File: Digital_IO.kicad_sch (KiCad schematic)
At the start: 28 parts, among them J1 MMCX, J10 MMCX, J11 MMCX, J12 MMCX, J13 MMCX, J14 MMCX, J15 MMCX, J16 MMCX, J2 MMCX, J3 MMCX, J4 MMCX, J5 MMCX, J6 MMCX, J7 MMCX, J8 MMCX, J9 MMCX, U44 LP3855EMP-ADJ/NOPB

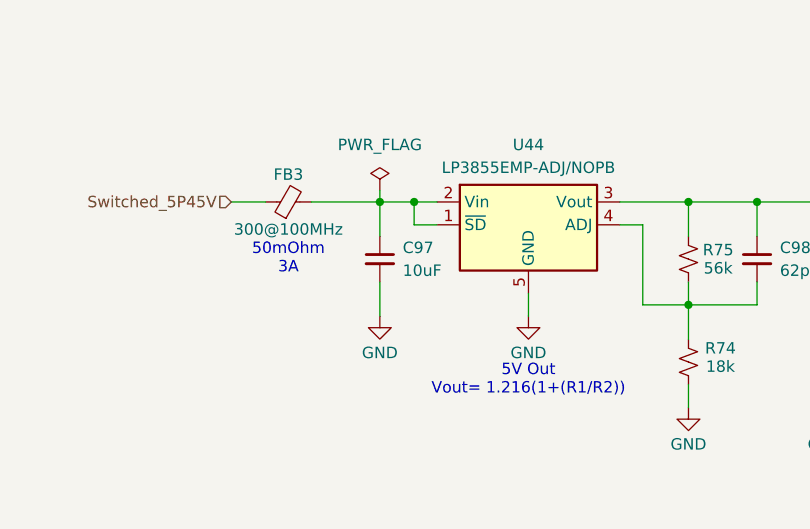
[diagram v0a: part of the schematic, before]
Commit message: Modified Power Filtering
- Removed FB1 & C136
- Added additional 1210 bypassing caps on main power inputs from FMC
- Changed SMPS output caps to the new 1210 22uF part
- Changed Input cap to LD0 U44 to the new 22uF part.
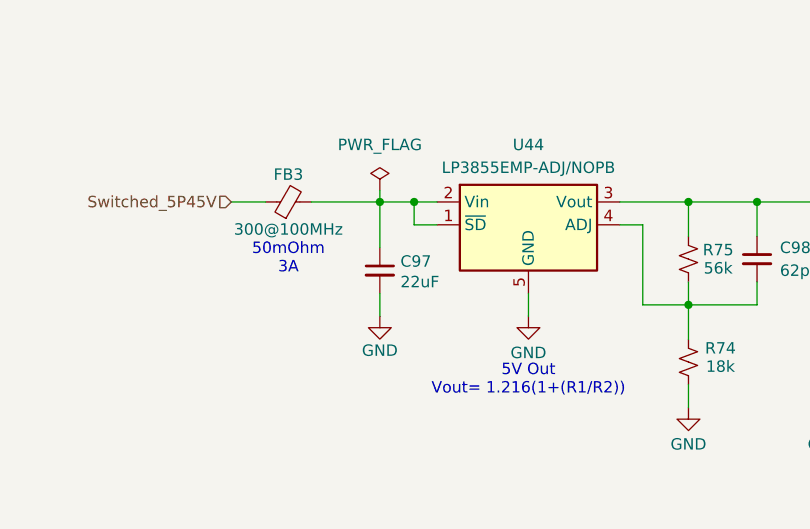
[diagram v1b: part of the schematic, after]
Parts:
- C97: value 10uF -> 22uF; footprint Capacitor_SMD:C_0805_2012Metric -> Capacitor_SMD:C_1210_3225Metric; MPN GRM21BR61E106KA73L -> CL32A226KAJNNWE; Manufacturer Murata -> Samsung Electro-Mechanics
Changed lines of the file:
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@@
 	(wire
 		(pts
+			(xy 54.61 137.16) (xy 54.61 139.7)
+		)
+		(stroke
+			(width 0)
+			(type default)
+		)
+	)
+	(wire
+		(pts
 			(xy 243.84 92.71) (xy 237.49 92.71)
 		)
@@
 	(wire
 		(pts
-			(xy 54.61 135.89) (xy 54.61 139.7)
-		)
-		(stroke
-			(width 0)
-			(type default)
-		)
-	)
-	(wire
-		(pts
 			(xy 219.71 113.03) (xy 215.9 113.03)
 		)
@@
 		)
 	)
+	(wire
+		(pts
+			(xy 54.61 127) (xy 54.61 132.08)
+		)
+		(stroke
+			(width 0)
+			(type default)
+		)
+	)
 	(bus
 		(pts
@@
 	(wire
 		(pts
-			(xy 54.61 127) (xy 54.61 130.81)
-		)
-		(stroke
-			(width 0)
-			(type default)
-		)
-	)
-	(wire
-		(pts
 			(xy 96.52 138.43) (xy 88.9 138.43)
 		)
@@
 	)
 	(symbol
-		(lib_id "power:GND")
-		(at 54.61 139.7 0)
-		(unit 1)
-		(exclude_from_sim no)
-		(in_bom yes)
-		(on_board yes)
-		(dnp no)
-		(property "Reference" "#PWR0105"
-			(at 54.61 146.05 0)
-			(effects
-				(font
-					(size 1.27 1.27)
-				)
-				(hide yes)
-			)
-		)
-		(property "Value" "GND"
-			(at 54.61 143.764 0)
-			(effects
-				(font
-					(size 1.27 1.27)
-				)
-			)
-		)
-		(property "Footprint" ""
-			(at 54.61 139.7 0)
-			(effects
-				(font
-					(size 1.27 1.27)
-				)
-				(hide yes)
-			)
-		)
-		(property "Datasheet" ""
-			(at 54.61 139.7 0)
-			(effects
-				(font
-					(size 1.27 1.27)
-				)
-				(hide yes)
-			)
-		)
-		(property "Description" "Power symbol creates a global label with name \"GND\" , ground"
-			(at 54.61 139.7 0)
-			(effects
-				(font
-					(size 1.27 1.27)
-				)
-				(hide yes)
-			)
-		)
-		(pin "1"
-		)
-		(instances
-			(project "trigger-output-fmc"
-				(path "/1719e569-47c8-4fa0-8523-9c9686ef0dba/e8674f3d-4c31-47ac-9c13-b31bc6bb3cc0"
-					(reference "#PWR0105")
-					(unit 1)
-				)
-			)
-		)
-	)
-	(symbol
 		(lib_id "Connector:Conn_Coaxial_Small")
 		(at 213.36 95.25 0)
@@
 	)
 	(symbol
-		(lib_id "Device:C_Small")
-		(at 54.61 133.35 0)
-		(unit 1)
-		(exclude_from_sim no)
-		(in_bom yes)
-		(on_board yes)
-		(dnp no)
-		(fields_autoplaced yes)
-		(property "Reference" "C97"
-			(at 57.15 132.0862 0)
-			(effects
-				(font
-					(size 1.27 1.27)
-				)
-				(justify left)
-			)
-		)
-		(property "Value" "10uF"
-			(at 57.15 134.6262 0)
-			(effects
-				(font
-					(size 1.27 1.27)
-				)
-				(justify left)
-			)
-		)
-		(property "Footprint" "Capacitor_SMD:C_0805_2012Metric"
-			(at 54.61 133.35 0)
-			(effects
-				(font
-					(size 1.27 1.27)
-				)
-				(hide yes)
-			)
-		)
-		(property "Datasheet" "~"
-			(at 54.61 133.35 0)
-			(effects
-				(font
-					(size 1.27 1.27)
-				)
-				(hide yes)
-			)
-		)
-		(property "Description" "CAP CER 10UF 25V X5R 0805"
-			(at 54.61 133.35 0)
-			(effects
-				(font
-					(size 1.27 1.27)
-				)
-				(hide yes)
-			)
-		)
-		(property "MPN" "GRM21BR61E106KA73L"
-			(at 54.61 133.35 0)
-			(effects
-				(font
-					(size 1.27 1.27)
-				)
-				(hide yes)
-			)
-		)
-		(property "Manufacturer" "Murata"
-			(at 54.61 133.35 0)
-			(effects
-				(font
-					(size 1.27 1.27)
-				)
-				(hide yes)
-			)
-		)
-		(pin "2"
-		)
-		(pin "1"
-		)
-		(instances
-			(project "trigger-output-fmc"
-				(path "/1719e569-47c8-4fa0-8523-9c9686ef0dba/e8674f3d-4c31-47ac-9c13-b31bc6bb3cc0"
-					(reference "C97")
-					(unit 1)
-				)
-			)
-		)
-	)
-	(symbol
 		(lib_id "Connector:Conn_Coaxial_Small")
 		(at 213.36 113.03 0)
@@
 	)
 	(symbol
+		(lib_id "Device:C_Small")
+		(at 54.61 134.62 0)
+		(unit 1)
+		(exclude_from_sim no)
+		(in_bom yes)
+		(on_board yes)
+		(dnp no)
+		(property "Reference" "C97"
+			(at 56.896 133.604 0)
+			(effects
+				(font
+					(size 1.27 1.27)
+				)
+				(justify left)
+			)
+		)
+		(property "Value" "22uF"
+			(at 56.896 135.89 0)
+			(effects
+				(font
+					(size 1.27 1.27)
+				)
+				(justify left)
+			)
+		)
+		(property "Footprint" "Capacitor_SMD:C_1210_3225Metric"
+			(at 54.61 134.62 0)
+			(effects
+				(font
+					(size 1.27 1.27)
+				)
+				(hide yes)
+			)
+		)
+		(property "Datasheet" "~"
+			(at 54.61 134.62 0)
+			(effects
+				(font
+					(size 1.27 1.27)
+				)
+				(hide yes)
+			)
+		)
+		(property "Description" "CAP CER 22UF 25V X5R 1210"
+			(at 54.61 134.62 0)
+			(effects
+				(font
+					(size 1.27 1.27)
+				)
+				(hide yes)
+			)
+		)
+		(property "MPN" "CL32A226KAJNNWE"
+			(at 54.61 134.62 0)
+			(effects
+				(font
+					(size 1.27 1.27)
+				)
+				(hide yes)
+			)
+		)
+		(property "Manufacturer" "Samsung Electro-Mechanics"
+			(at 54.61 134.62 0)
+			(effects
+				(font
+					(size 1.27 1.27)
+				)
+				(hide yes)
+			)
+		)
+		(pin "1"
+		)
+		(pin "2"
+		)
+		(instances
+			(project "trigger-output-fmc"
+				(path "/1719e569-47c8-4fa0-8523-9c9686ef0dba/e8674f3d-4c31-47ac-9c13-b31bc6bb3cc0"
+					(reference "C97")
+					(unit 1)
+				)
+			)
+		)
+	)
+	(symbol
 		(lib_id "Connector:Conn_Coaxial_Small")
 		(at 275.59 132.08 0)
@@
 					(unit 1)
 				)
+			)
+		)
+	)
+	(symbol
+		(lib_id "power:GND")
+		(at 54.61 139.7 0)
+		(unit 1)
+		(exclude_from_sim no)
+		(in_bom yes)
+		(on_board yes)
+		(dnp no)
+		(property "Reference" "#PWR097"
+			(at 54.61 146.05 0)
+			(effects
+				(font
+					(size 1.27 1.27)
+				)
+				(hide yes)
+			)
+		)
+		(property "Value" "GND"
+			(at 54.61 143.51 0)
+			(effects
+				(font
+					(size 1.27 1.27)
+				)
+			)
+		)
+		(property "Footprint" ""
+			(at 54.61 139.7 0)
+			(effects
+				(font
+					(size 1.27 1.27)
+				)
+				(hide yes)
+			)
+		)
+		(property "Datasheet" ""
+			(at 54.61 139.7 0)
+			(effects
+				(font
+					(size 1.27 1.27)
+				)
+				(hide yes)
+			)
+		)
+		(property "Description" "Power symbol creates a global label with name \"GND\" , ground"
+			(at 54.61 139.7 0)
+			(effects
+				(font
+					(size 1.27 1.27)
+				)
+				(hide yes)
+			)
+		)
+		(pin "1"
+		)
+		(instances
+			(project "trigger-output-fmc"
+				(path "/1719e569-47c8-4fa0-8523-9c9686ef0dba/e8674f3d-4c31-47ac-9c13-b31bc6bb3cc0"
+					(reference "#PWR097")
+					(unit 1)
+				)

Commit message: Changes to Power Filtering
- Removed extra bulk caps on FMC power inputs
- Cleaned up some power routing between U22 & U44
- Made some vias larger for power tree connections
- Changed 22uF to a new 35V part
- Changed 10uF part to a new equivalent part due to OOS.
- Modified text near U27 on schematic for clarity
- Added notes on the power schematics showing effective capacitance of chosen bulk mlcc caps
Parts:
- C101, C102, C103, C95, C96: MPN GRM21BR61E106KA73L -> TMK212BBJ106MG-T; Manufacturer Murata -> Taiyo Yuden
- C97: MPN CL32A226KAJNNWE -> GMK325BJ226MM-P; Manufacturer Samsung Electro-Mechanics -> Taiyo Yuden
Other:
- note added: "~20uF effective @5.45VDC"
- note added: "~6uF/ea effective @5VDC"
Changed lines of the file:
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@@
 		(comment 1 "SPDX-License-Identifier: CERN-OHL-S-2.0+")
 	)
+	(text "~20uF effective @5.45VDC"
+		(exclude_from_sim no)
+		(at 54.61 145.542 0)
+		(effects
+			(font
+				(size 1.27 1.27)
+			)
+		)
+	)
 	(text "5V Out\nVout= 1.216(1+(R1/R2))"
 		(exclude_from_sim no)
-		(at 71.12 146.812 0)
+		(at 95.758 122.174 0)
 		(effects
 			(font
@@
 		)
 	)
+	(text "~6uF/ea effective @5VDC"
+		(exclude_from_sim no)
+		(at 120.904 156.718 0)
+		(effects
+			(font
+				(size 1.27 1.27)
+			)
+		)
+	)
 	(junction
 		(at 280.67 114.3)
@@
 			)
 		)
-		(property "MPN" "GRM21BR61E106KA73L"
+		(property "MPN" "TMK212BBJ106MG-T"
 			(at 125.73 138.43 0)
 			(effects
@@
 			)
 		)
-		(property "Manufacturer" "Murata"
+		(property "Manufacturer" "Taiyo Yuden"
 			(at 125.73 138.43 0)
 			(effects
@@
 			)
 		)
-		(property "MPN" "GRM21BR61E106KA73L"
+		(property "MPN" "TMK212BBJ106MG-T"
 			(at 134.62 138.43 0)
 			(effects
@@
 			)
 		)
-		(property "Manufacturer" "Murata"
+		(property "Manufacturer" "Taiyo Yuden"
 			(at 134.62 138.43 0)
 			(effects
@@
 			)
 		)
-		(property "MPN" "GRM21BR61E106KA73L"
+		(property "MPN" "TMK212BBJ106MG-T"
 			(at 104.14 138.43 0)
 			(effects
@@
 			)
 		)
-		(property "Manufacturer" "Murata"
+		(property "Manufacturer" "Taiyo Yuden"
 			(at 104.14 138.43 0)
 			(effects
@@
 			)
 		)
-		(property "MPN" "GRM21BR61E106KA73L"
+		(property "MPN" "TMK212BBJ106MG-T"
 			(at 115.57 138.43 0)
 			(effects
@@
 			)
 		)
-		(property "Manufacturer" "Murata"
+		(property "Manufacturer" "Taiyo Yuden"
 			(at 115.57 138.43 0)
 			(effects
@@
 			)
 		)
-		(property "Description" "CAP CER 22UF 25V X5R 1210"
+		(property "Description" "CAP CER 22UF 35V X5R 1210"
 			(at 54.61 134.62 0)
 			(effects
@@
 			)
 		)
-		(property "MPN" "CL32A226KAJNNWE"
+		(property "MPN" "GMK325BJ226MM-P"
 			(at 54.61 134.62 0)
 			(effects
@@
 			)
 		)
-		(property "Manufacturer" "Samsung Electro-Mechanics"
+		(property "Manufacturer" "Taiyo Yuden"
 			(at 54.61 134.62 0)
 			(effects
@@
 			)
 		)
-		(property "MPN" "GRM21BR61E106KA73L"
+		(property "MPN" "TMK212BBJ106MG-T"
 			(at 143.51 138.43 0)
 			(effects
@@
 			)
 		)
-		(property "Manufacturer" "Murata"
+		(property "Manufacturer" "Taiyo Yuden"
 			(at 143.51 138.43 0)
 			(effects
